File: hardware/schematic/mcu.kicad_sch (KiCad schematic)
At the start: 52 parts, among them J10 5.0-2P, J11 2.54-2P, J12 2.54-2P, J13 2.54-2P, J14 2.54-2P, J15 2.54-2X6P, J9 5.0-2P, Q1 HYG017N04LS1C2, Q2 HYG017N04LS1C2, SW3 TSA016A2518A, SW4 TSA016A2518A, U10 TJA1051TK/3/1J, U11 RP2040, U8 W25Q16JVUXIQ, U9 ADXL345BCCZ, X2 X322512MSB4SI

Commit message: feat: upload rev 3.1 schematic
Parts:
- J10, J9: value 5.0-2P -> DB301V-5.0-2P; LCSC Part (none) -> C395882
- J11, J12, J13, J14: value 2.54-2P -> 2.54-2P ZZDK; LCSC Part (none) -> C18185649
- J15: value 2.54-2X6P -> KH-2.54PH180-2X6P-L8.9; LCSC Part (none) -> C5157629
- TP15, TP16, TP17, TP18: now in the parts list
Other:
- moved on the sheet: C28, C31, C33, J11, J12, J13, J14, Q1, Q2, R20, R23, R24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

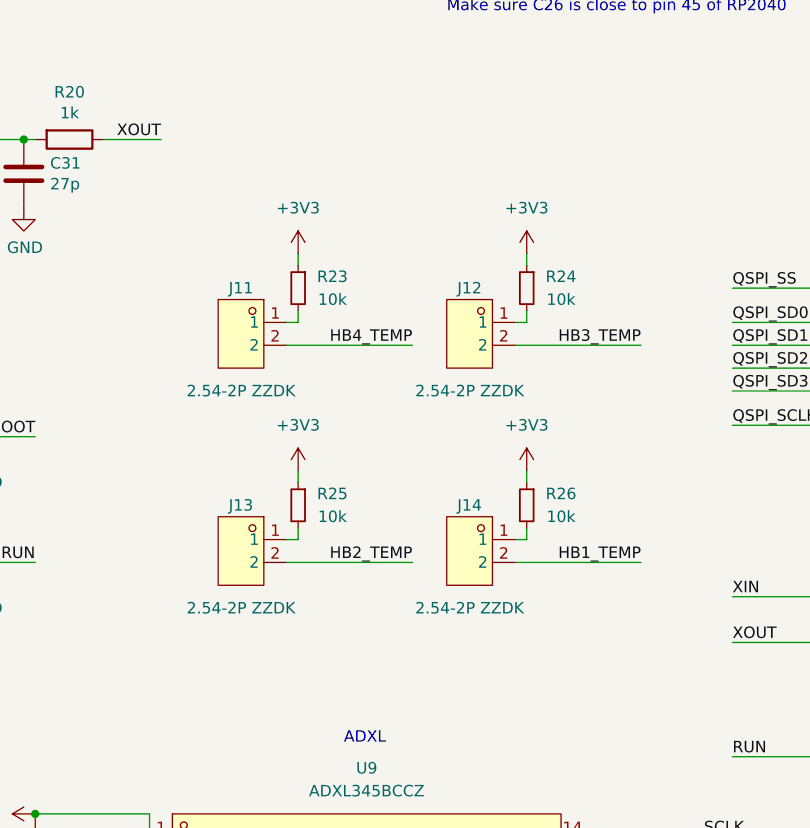
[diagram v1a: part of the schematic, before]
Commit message: fix: correct thermistor wiring
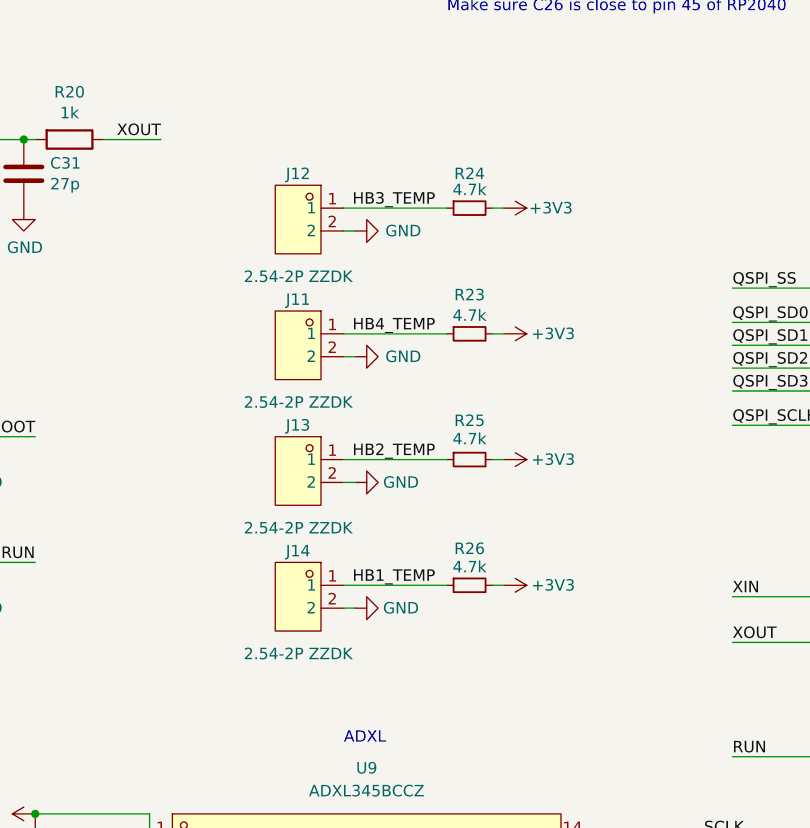
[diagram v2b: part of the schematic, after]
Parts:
- R23, R24, R25, R26: value 10k -> 4.7k
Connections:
- net +3V3: now also R23.2, R24.2, R25.2, R26.2; no longer R23.1, R24.1, R25.1, R26.1
- net GND: now also J11.2, J12.2, J13.2, J14.2
- net HB1_TEMP: now also J14.1, R26.1; no longer J14.2
- net HB2_TEMP: now also J13.1, R25.1; no longer J13.2
- net HB3_TEMP: now also J12.1, R24.1; no longer J12.2
- net HB4_TEMP: now also J11.1, R23.1; no longer J11.2
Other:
- moved on the sheet: J11, J12, J13, J14, R23, R24, R25, R26
